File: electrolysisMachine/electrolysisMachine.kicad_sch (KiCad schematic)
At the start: 25 parts

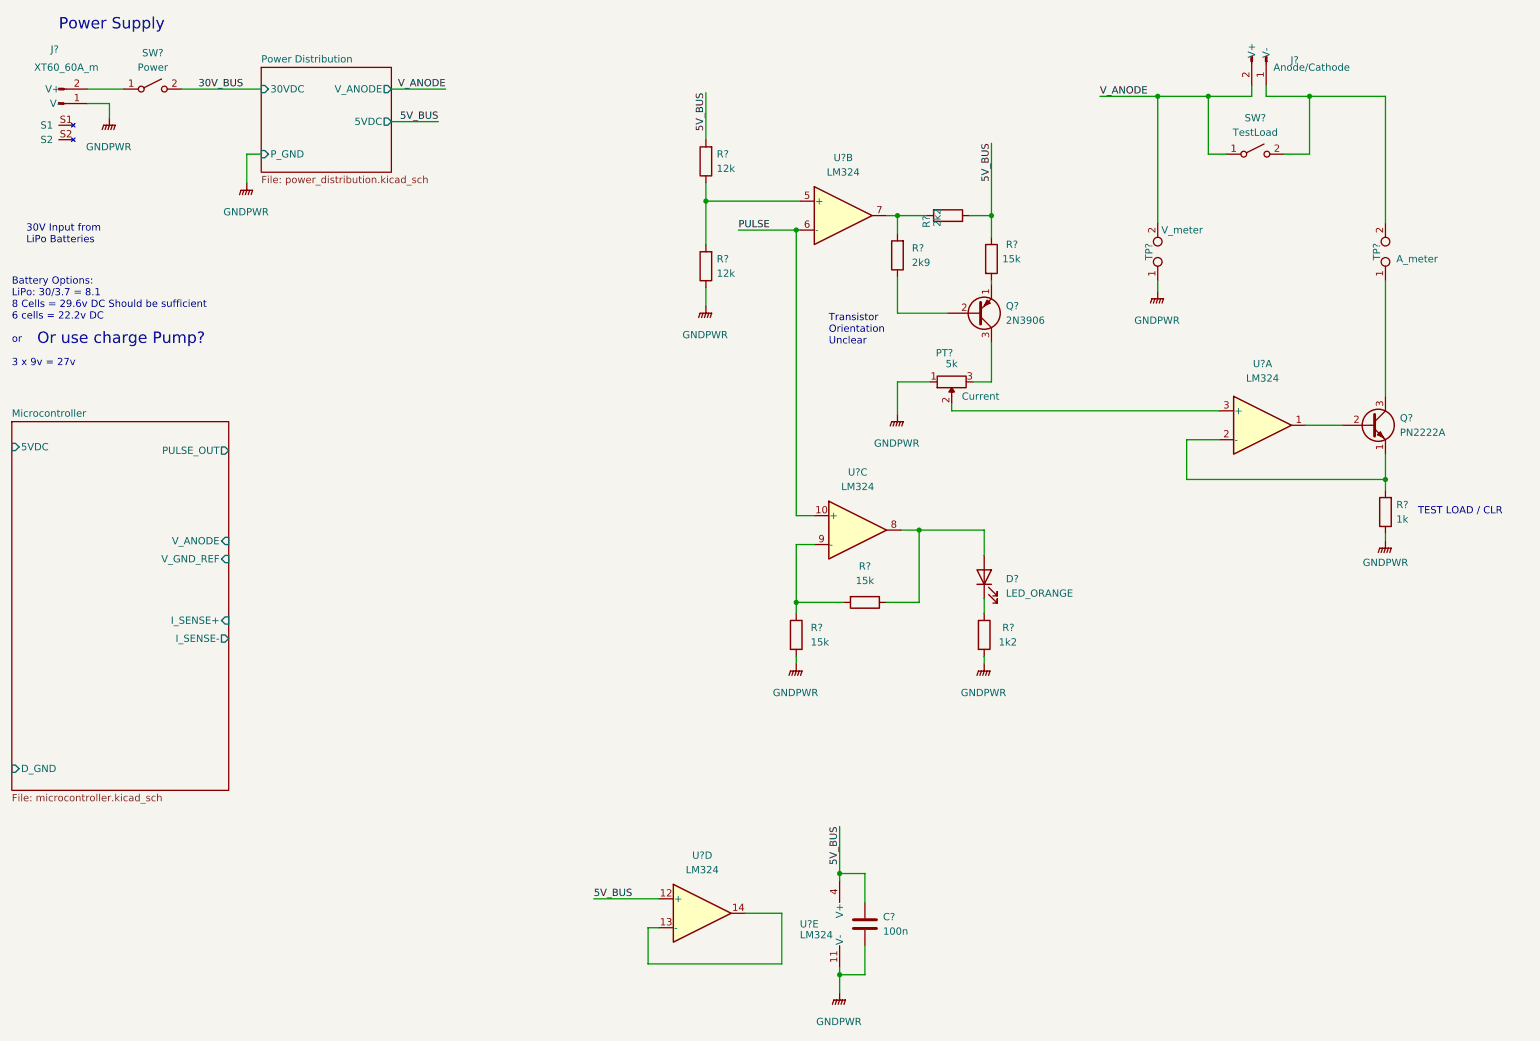
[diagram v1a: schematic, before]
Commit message: updated kicad schematic
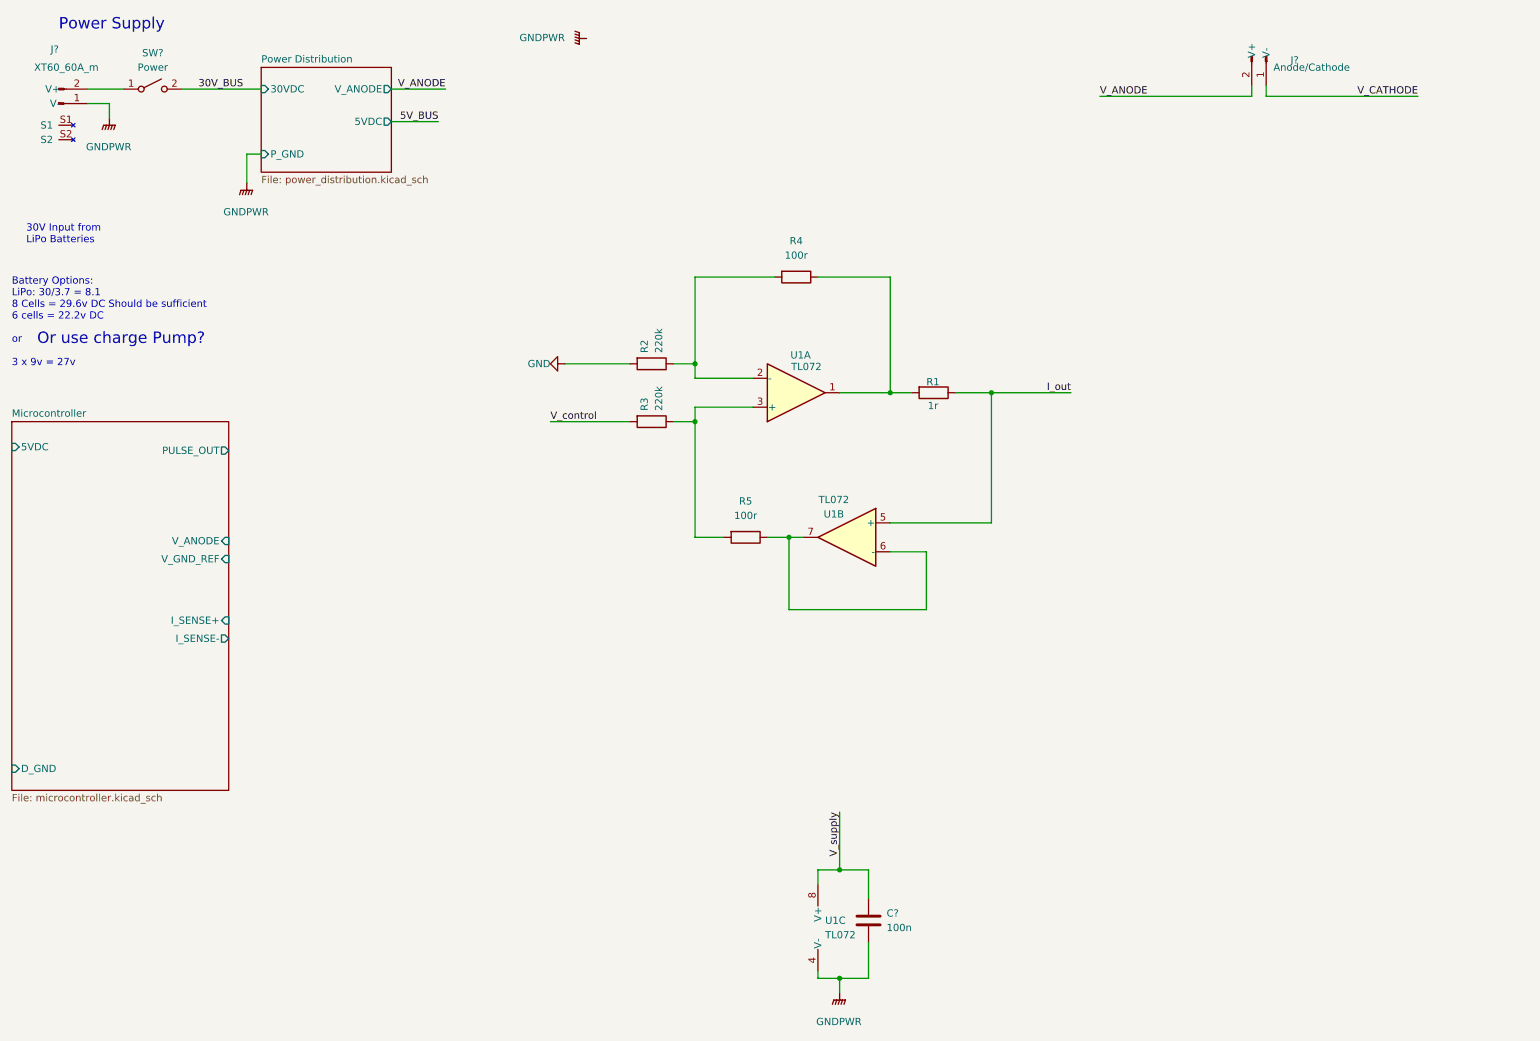
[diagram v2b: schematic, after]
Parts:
- removed D?: LED_ORANGE, Diode_SMD:D_0805_2012Metric_Pad1.15x1.40mm_HandSolder, symbol 000_Diodes_Immo:LED_0805_smd
- removed PT?: 5k, Potentiometer_THT:Potentiometer_Alpha_RD901F-40-00D_Single_Vertical_CircularHoles, symbol 000_Resistors_Immo:Potentiometer
- removed Q?: PN2222A, Package_TO_SOT_THT:TO-92_Inline, symbol Transistor_BJT:PN2222A
- removed Q?: 2N3906, Package_TO_SOT_THT:TO-92_Inline, symbol Transistor_BJT:2N3906
- removed R? (x2): 12k, Resistor_SMD:R_0805_2012Metric_Pad1.20x1.40mm_HandSolder, symbol 000_Resistors_Immo:Resistor_0805
- removed R?: 1k2, Resistor_SMD:R_0805_2012Metric_Pad1.20x1.40mm_HandSolder, symbol 000_Resistors_Immo:Resistor_0805
- removed R?: 2k9, Resistor_SMD:R_0805_2012Metric_Pad1.20x1.40mm_HandSolder, symbol 000_Resistors_Immo:Resistor_0805
- removed R? (x3): 15k, Resistor_SMD:R_0805_2012Metric_Pad1.20x1.40mm_HandSolder, symbol 000_Resistors_Immo:Resistor_0805
- removed R?: 1k, Resistor_SMD:R_0805_2012Metric_Pad1.20x1.40mm_HandSolder, symbol 000_Resistors_Immo:Resistor_0805
- removed R?: 2k2, Resistor_SMD:R_0805_2012Metric_Pad1.20x1.40mm_HandSolder, symbol 000_Resistors_Immo:Resistor_0805
- removed SW?: TestLoad, symbol Switch:SW_SPST
- removed TP?: A_meter, symbol Connector:TestPoint_2Pole
- removed TP?: V_meter, symbol Connector:TestPoint_2Pole
- removed U? (x5): LM324, symbol Amplifier_Operational:LM324
- added R1: 1r, Resistor_SMD:R_0805_2012Metric_Pad1.20x1.40mm_HandSolder, symbol 000_Resistors_Immo:Resistor_0805
- added R2, R3: 220k, Resistor_SMD:R_0805_2012Metric_Pad1.20x1.40mm_HandSolder, symbol 000_Resistors_Immo:Resistor_0805
- added R4, R5: 100r, Resistor_SMD:R_0805_2012Metric_Pad1.20x1.40mm_HandSolder, symbol 000_Resistors_Immo:Resistor_0805
- added U1: TL072, symbol Amplifier_Operational:TL072
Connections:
- net 5V_BUS: no longer C?.1
- net GNDPWR: now also U1.4 (V-)
- net V_CATHODE: now reaches J?.1 (V-)
- new net: R2.1, R4.2, U1.2 (-)
- new net: R1.2, R4.1, U1.1
- new net: R3.1, R5.2, U1.3 (+)
- new net: R5.1, U1.6 (-), U1.7
- new net GND: R2.2
- new net I_out: R1.1, U1.5 (+)
- new net V_control: R3.2
- new net V_supply: C?.1, U1.8 (V+)
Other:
- note removed: "TEST LOAD / CLR"
- note removed: "Transistor Orientation Unclear"
- moved on the sheet: C?
